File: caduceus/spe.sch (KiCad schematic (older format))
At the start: 37 parts

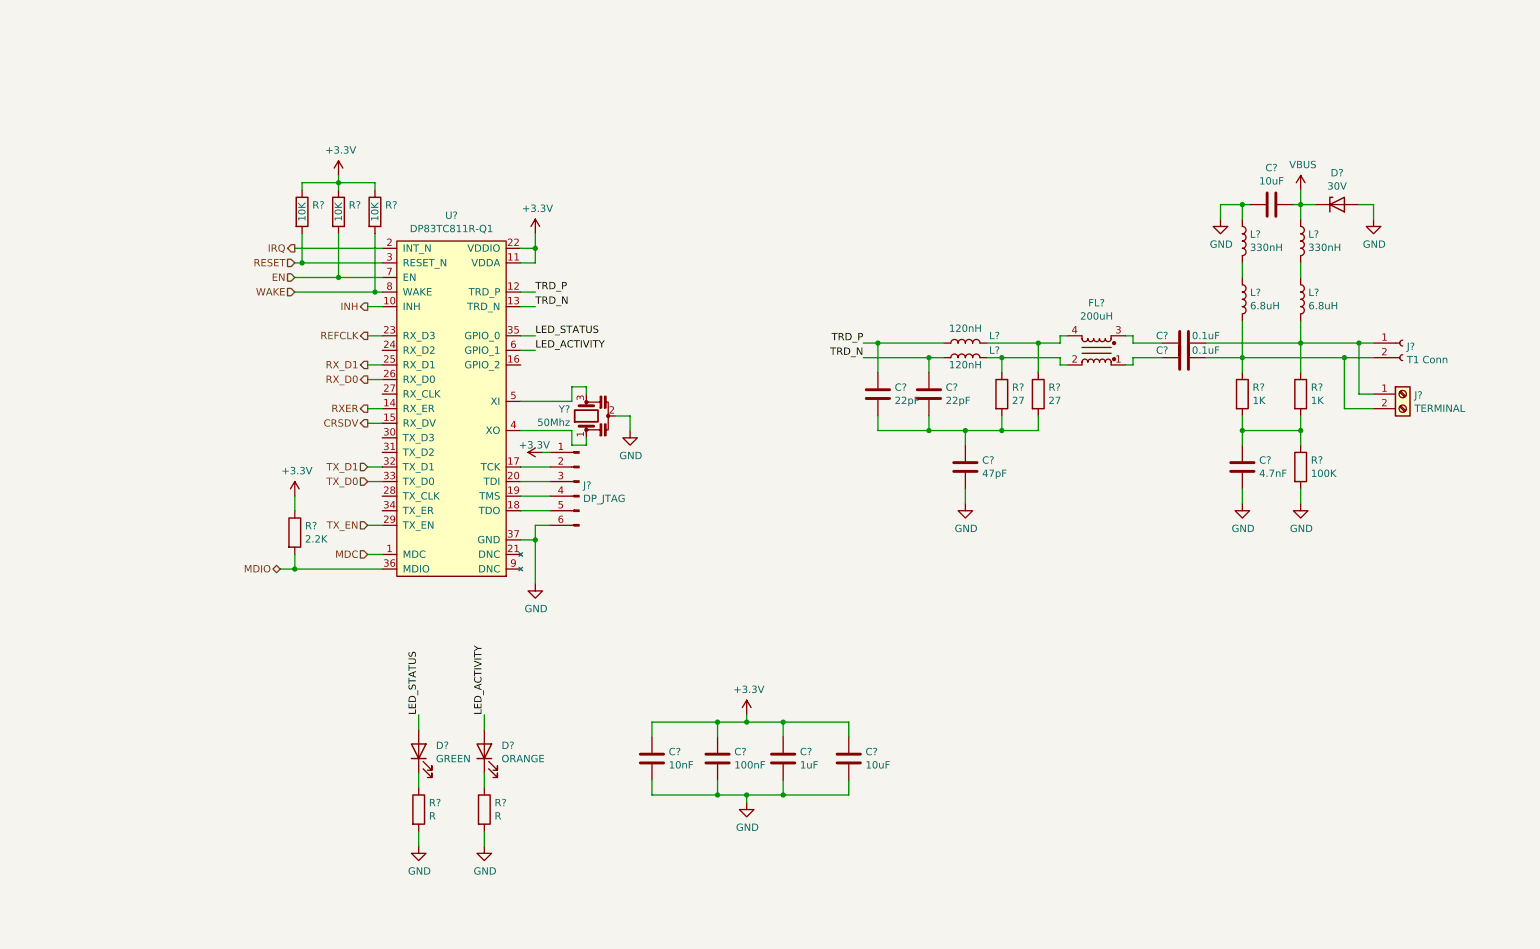
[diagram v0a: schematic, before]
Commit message: Added USB, resolved regulation, added headers, updated apperance of ethernet interface, added QSPI flash. Meant to add to devel branch but happened on master. Schematic basically done, requires review
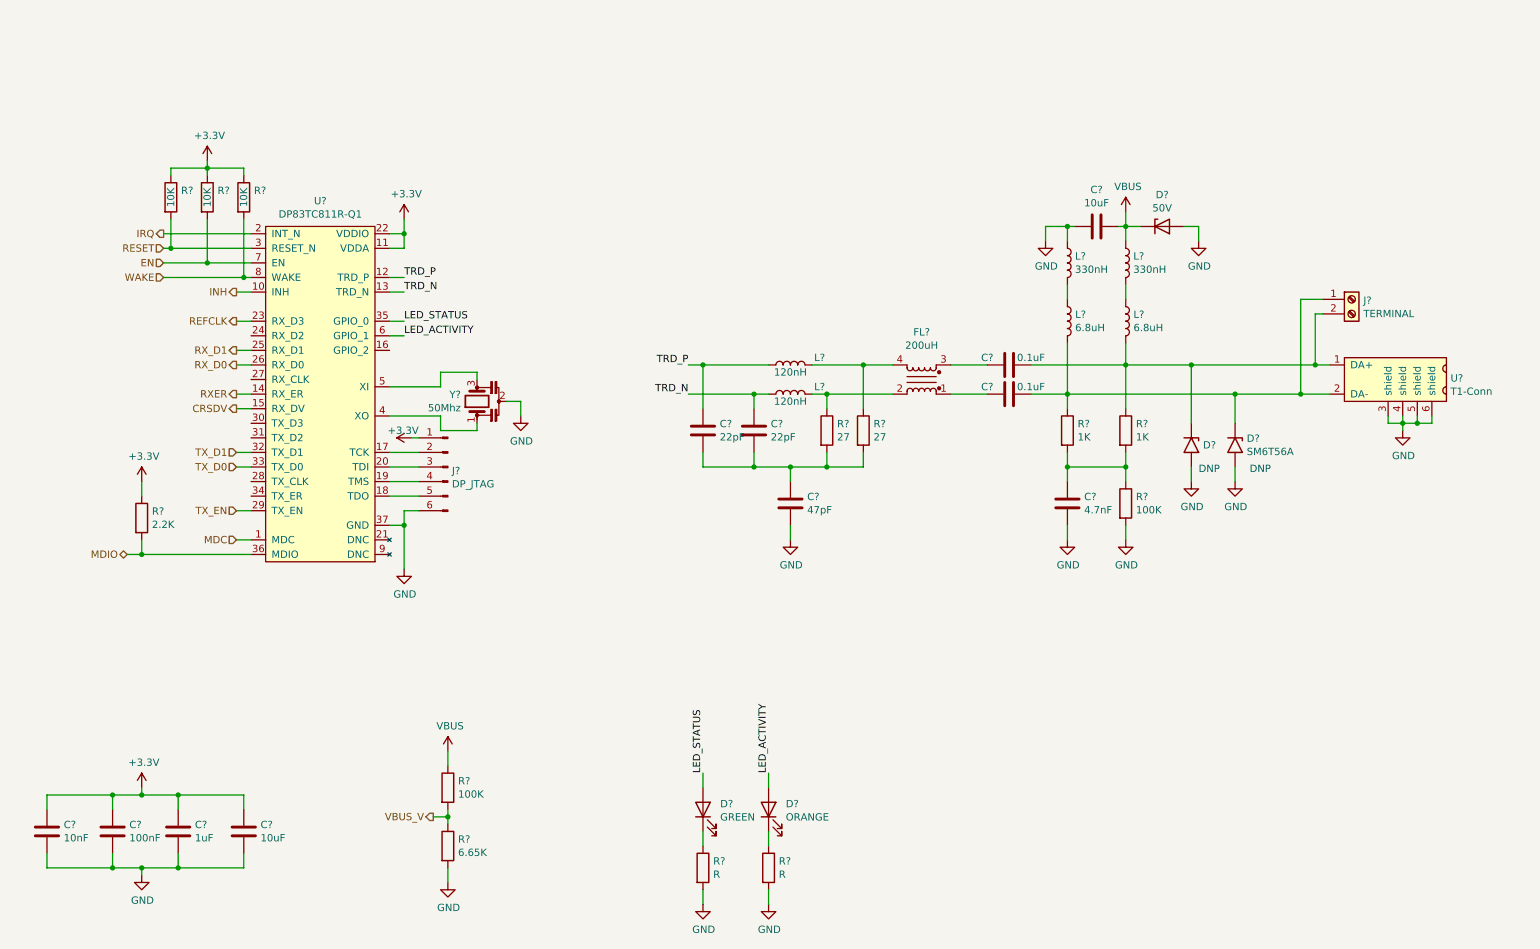
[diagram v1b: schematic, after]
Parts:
- removed J?: T1 Conn, symbol Connector:Conn_01x02_Female
- added D? (x2): SM6T56A, Diode_SMD:D_SMB, symbol Diode:SM6T56A
- added R?: 100K, symbol Device:R
- added R?: 6.65K, symbol Device:R
- added U?: T1-Conn, symbol caduceus:T1-Conn
- D?: value 30V -> 50V
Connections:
- net GND: now also D?.2 (A2), D?.2 (A2), R?.2, U?.3 (shield), U?.4 (shield), U?.5 (shield), U?.6 (shield)
- net VBUS: now also R?.1
- net at C?.1, L?.2, R?.1: now also J?.2 (Pin_2), D?.1 (A1), U?.1 (DA+); no longer J?.1 (Pin_1)
- net at C?.1, L?.2, R?.1: now also J?.1 (Pin_1), D?.1 (A1), U?.2 (DA-); no longer J?.2 (Pin_2)
- new net VBUS_V: R?.1, R?.2
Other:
- note added: "DNP"
- moved on the sheet: C?, D?, FL?, J?, L?, R?, U?, Y?

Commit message: Footprints done, not all are final
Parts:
- C21, C22, C23, C24: renamed from C?; footprint (none) -> Capacitor_SMD:C_0603_1608Metric
- C25, C26, C27, C28, C29, C30, C31: renamed from C?; footprint (none) -> Capacitor_SMD:C_0805_2012Metric
- D6: renamed from D?; PN (none) -> LTST-C171GKT
- D7: renamed from D?; PN (none) -> LTST-C170KFKT
- D8: renamed from D?; footprint (none) -> Diode_SMD:D_SOD-128
- FL1: renamed from FL?; footprint (none) -> Inductor_THT:L_CommonMode_Wuerth_WE-CMB-XS
- J5: renamed from J?; footprint (none) -> TerminalBlock:TerminalBlock_bornier-2_P5.08mm
- L3, L4, L5, L7: renamed from L?; footprint (none) -> Inductor_SMD:L_0805_2012Metric
- L6: renamed from L?; footprint (none) -> Inductor_SMD:L_Coilcraft_XxL4040
- R11, R12, R13, R14, R15, R16, R17, R18, R19, R20, R21, R22, R23: renamed from R?; footprint (none) -> Resistor_SMD:R_0603_1608Metric
- U4: renamed from U?; footprint (none) -> caduceus:VQFN-6x6mm-0.5p
- U5: renamed from U?; footprint (none) -> caduceus:T1-09452800
- gave numbers to parts that had none: 5

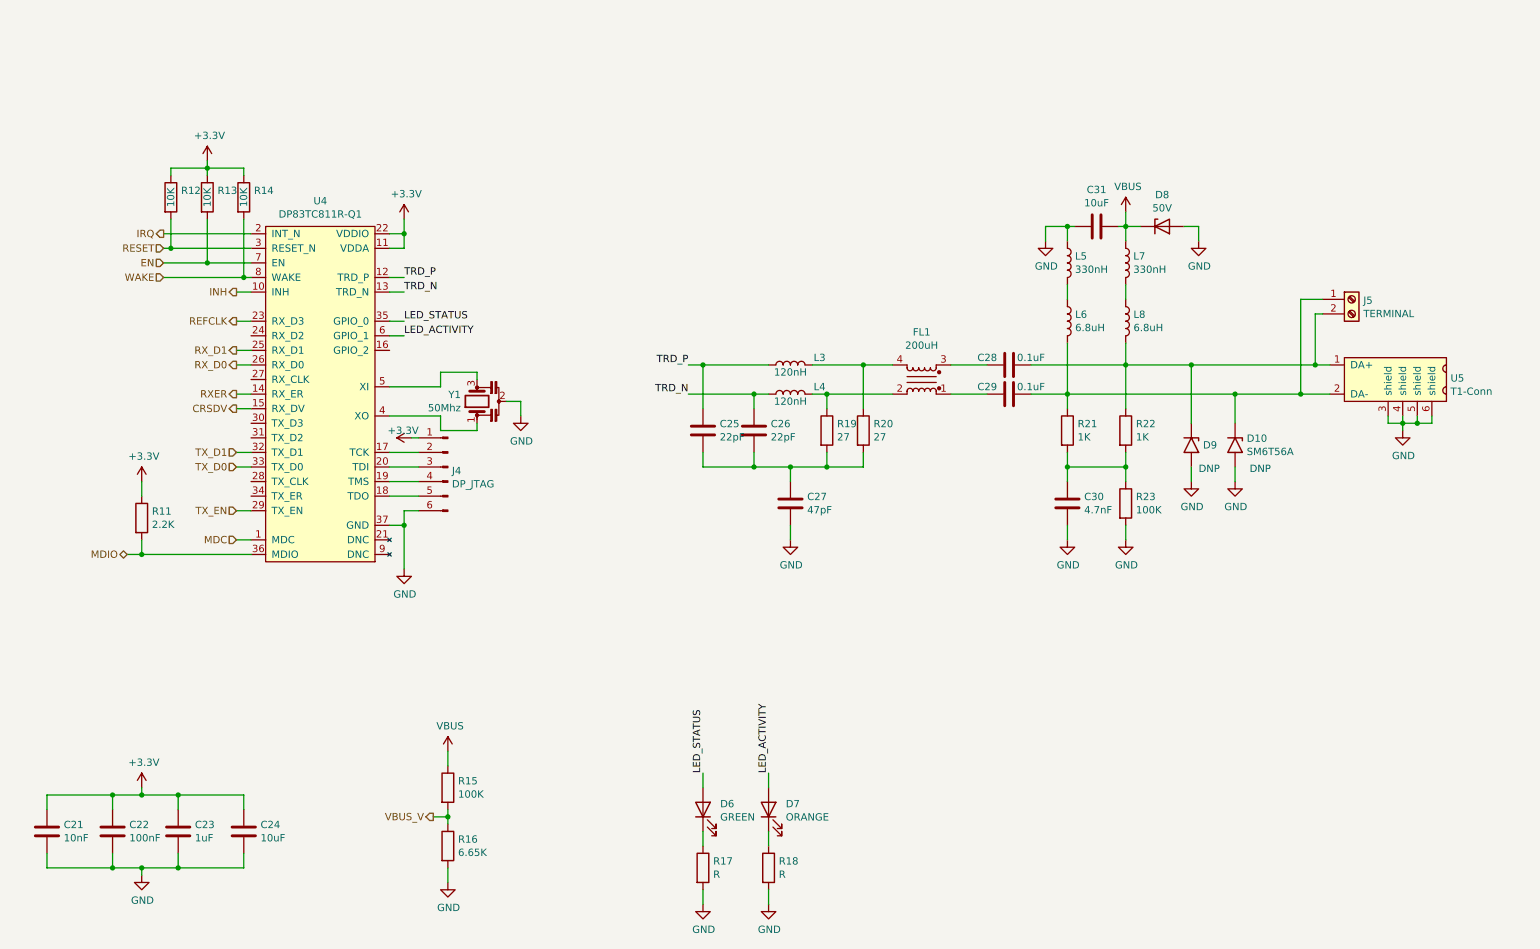
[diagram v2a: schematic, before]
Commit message: Changed PHY IC to DP83TD510E
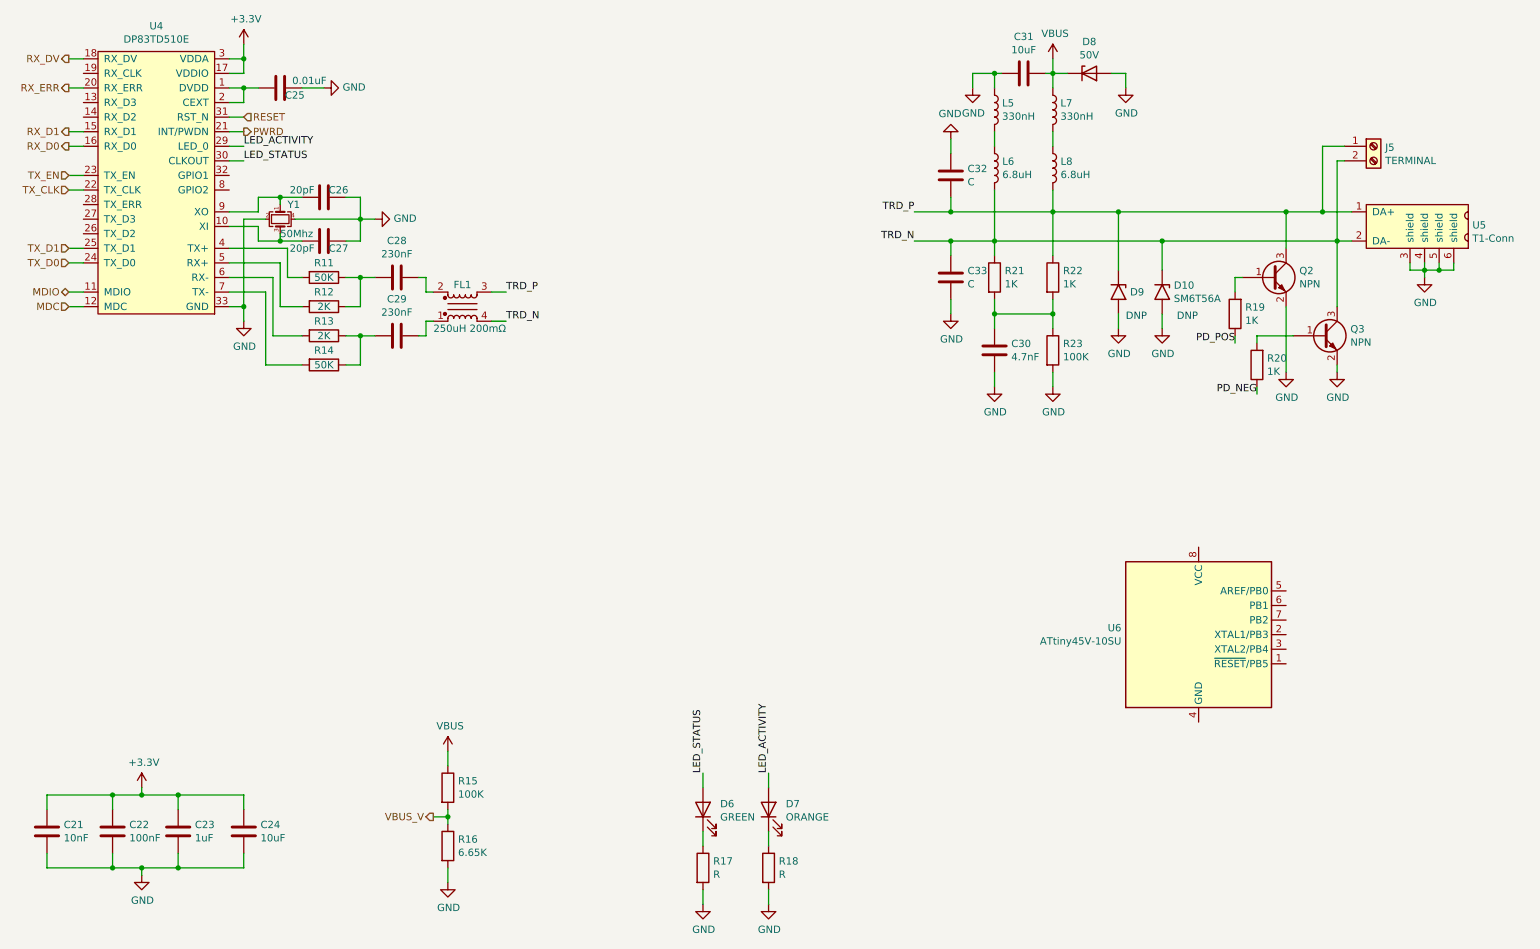
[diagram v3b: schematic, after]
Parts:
- removed FL1: 200uH, Inductor_THT:L_CommonMode_Wuerth_WE-CMB-XS, symbol Device:EMI_Filter_CommonMode
- removed J4: DP_JTAG, symbol Connector:Conn_01x06_Male
- removed L3, L4: 120nH, Inductor_SMD:L_0805_2012Metric, symbol Device:L
- removed U4: DP83TC811R-Q1, caduceus:VQFN-6x6mm-0.5p, symbol caduceus:DP83TC811R-Q1
- removed Y1: 50Mhz, symbol Device:Resonator
- added C32, C33: C, symbol Device:C
- added FL1: 250uH 200mΩ, symbol Device:EMI_Filter_LL_1423
- added Q2, Q3: NPN, symbol Device:Q_NPN_BEC
- added U4: DP83TD510E, symbol caduceus:DP83TD510E
- added U6: ATtiny45V-10SU, Package_SO:SOIJ-8_5.3x5.3mm_P1.27mm, symbol MCU_Microchip_ATtiny:ATtiny45V-10SU
- added Y1: 50Mhz, symbol Device:Crystal_GND24_Small
- C25: value 22pF -> 0.01uF; footprint Capacitor_SMD:C_0805_2012Metric -> (none)
- C26: value 22pF -> 20pF; footprint Capacitor_SMD:C_0805_2012Metric -> (none)
- C27: value 47pF -> 20pF; footprint Capacitor_SMD:C_0805_2012Metric -> (none)
- C28, C29: value 0.1uF -> 230nF; footprint Capacitor_SMD:C_0805_2012Metric -> (none)
- C30, C31: footprint Capacitor_SMD:C_0805_2012Metric -> Capacitor_SMD:C_0603_1608Metric
- D10, D9: footprint Diode_SMD:D_SMB -> Diode_SMD:D_SOD-123
- D6, D7: footprint (none) -> LED_SMD:LED_0805_2012Metric
- D8: footprint Diode_SMD:D_SOD-128 -> Diode_SMD:D_SOD-123
- L6: footprint Inductor_SMD:L_Coilcraft_XxL4040 -> Inductor_SMD:L_Coilcraft_XxL4020
- L8: footprint (none) -> Inductor_SMD:L_Coilcraft_XxL4020
- R11: value 2.2K -> 50K; footprint Resistor_SMD:R_0603_1608Metric -> (none)
- R12, R13: value 10K -> 2K; footprint Resistor_SMD:R_0603_1608Metric -> (none)
- R14: value 10K -> 50K; footprint Resistor_SMD:R_0603_1608Metric -> (none)
- R19, R20: value 27 -> 1K; footprint Resistor_SMD:R_0603_1608Metric -> (none)
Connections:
- net +3V3: now also U4.17 (VDDIO), U4.3 (VDDA); no longer R11.1, R12.1, R13.1, R14.1
- net GND: now also C25.1, C26.1, C32.1, C33.2, Q2.2 (E), Q3.2 (E), U4.33 (GND), Y1.2, Y1.4
- net LED_ACTIVITY: now also U4.29 (LED_0)
- net LED_STATUS: now also U4.30 (CLKOUT)
- net MDC: now also U4.12 (MDC)
- net MDIO: now also U4.11 (MDIO); no longer R11.2
- net RESET: now also U4.31 (RST_N); no longer R12.2
- net RX_D0: now also U4.16 (RX_D0)
- net RX_D1: now also U4.15 (RX_D1)
- net TRD_N: now also D10.1 (A1), J5.2 (Pin_2), L6.2, R21.1, U5.2 (DA-), C33.1, FL1.4, Q3.3 (C); no longer C26.1
- net TRD_P: now also D9.1 (A1), J5.1 (Pin_1), L8.2, R22.1, U5.1 (DA+), C32.2, FL1.3, Q2.3 (C); no longer C25.1
- net TX_D0: now also U4.24 (TX_D0)
- net TX_D1: now also U4.25 (TX_D1)
- net TX_EN: now also U4.23 (TX_EN)
- net PD_NEG: now reaches R20.1
- net PD_POS: now reaches R19.1
- net at C28.2: now also R11.1, R12.1
- net at C29.2: now also R13.1, R14.1
- net EN: no longer names the net of R13.2
- net EN: now also U4.6 (RX-)
- net WAKE: no longer names the net of R14.2
- net WAKE: now also U4.7 (TX-)
- new net: C25.2, U4.1 (DVDD), U4.2 (CEXT)
- new net: C27.1, U4.10 (XI), Y1.3
- new net: R11.2, U4.4 (TX+)
- new net: R12.2, U4.5 (RX+)
- new net: C26.2, U4.9 (XO), Y1.1
- new net: Q2.1 (B), R19.2
- new net: Q3.1 (B), R20.2
- new net: C29.1, FL1.1
- new net: C28.1, FL1.2
- new net PWRD: U4.21 (INT/PWDN)
- new net RX_DV: U4.18 (RX_DV)
- new net RX_ERR: U4.20 (RX_ERR)
- new net TX_CLK: U4.22 (TX_CLK)
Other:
- moved on the sheet: C30, C31, D10, D8, D9, J5, L5, L6, L7, L8, R21, R22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
